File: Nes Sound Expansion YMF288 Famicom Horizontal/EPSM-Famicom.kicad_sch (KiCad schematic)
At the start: 39 parts

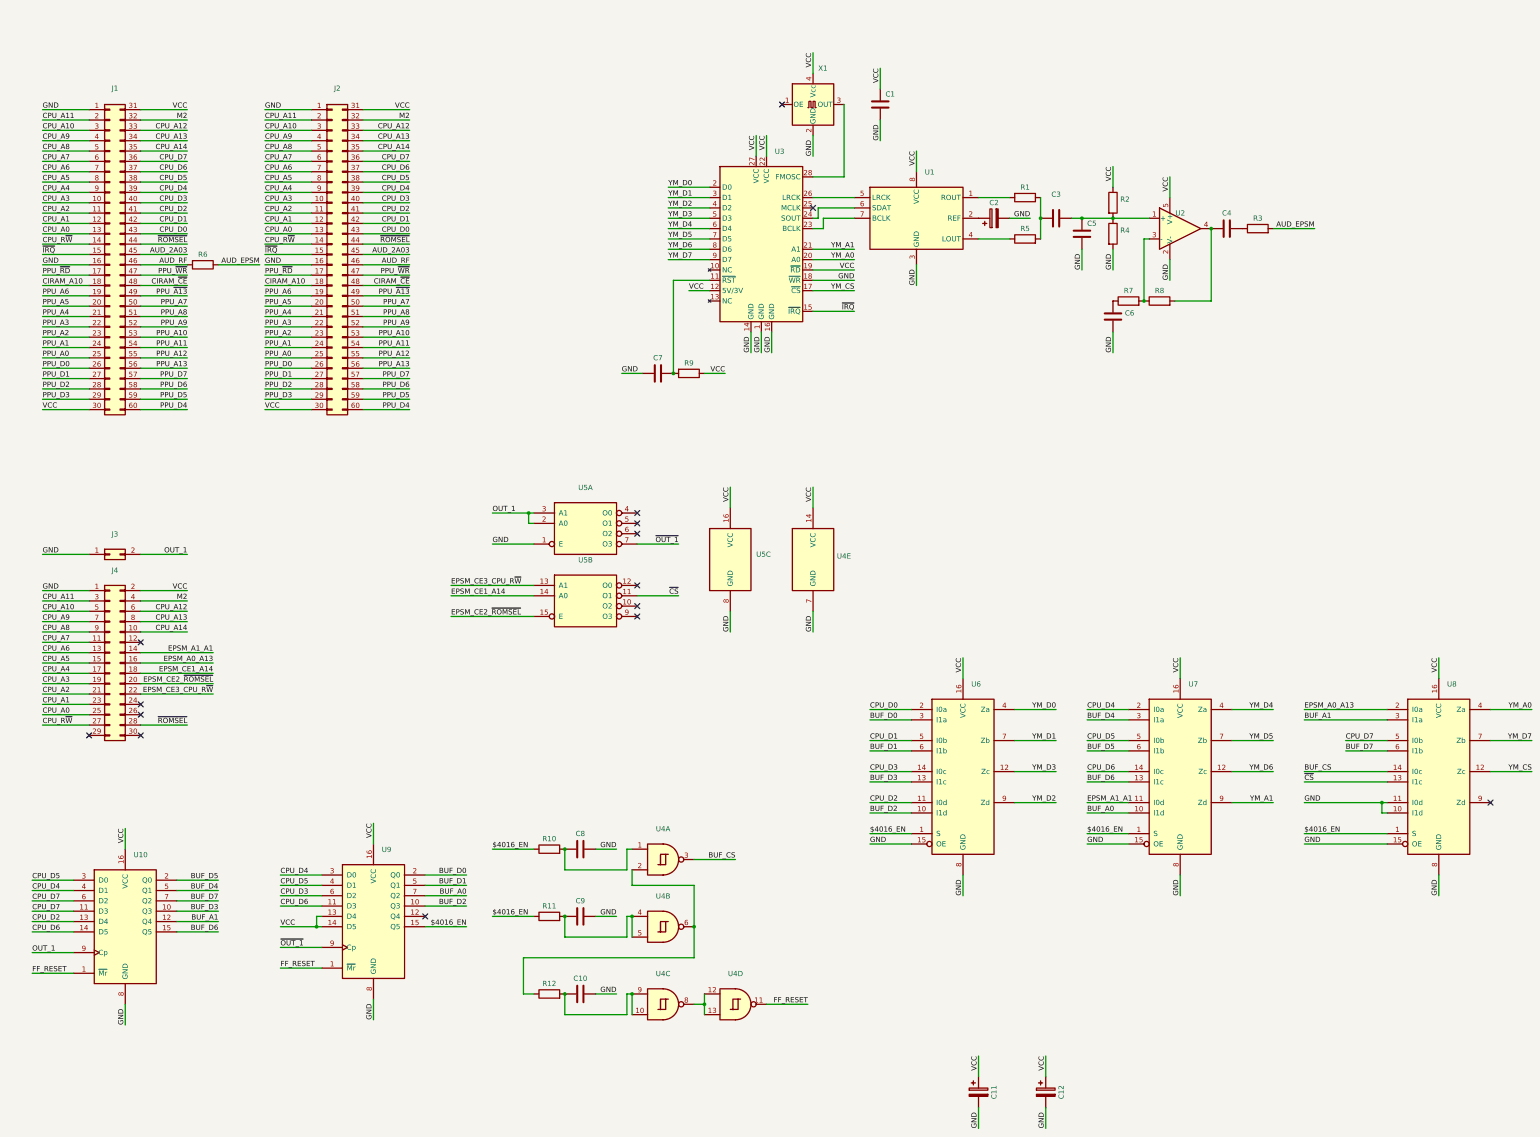
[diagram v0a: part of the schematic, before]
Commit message: Flip cartridge connection to back instead of front
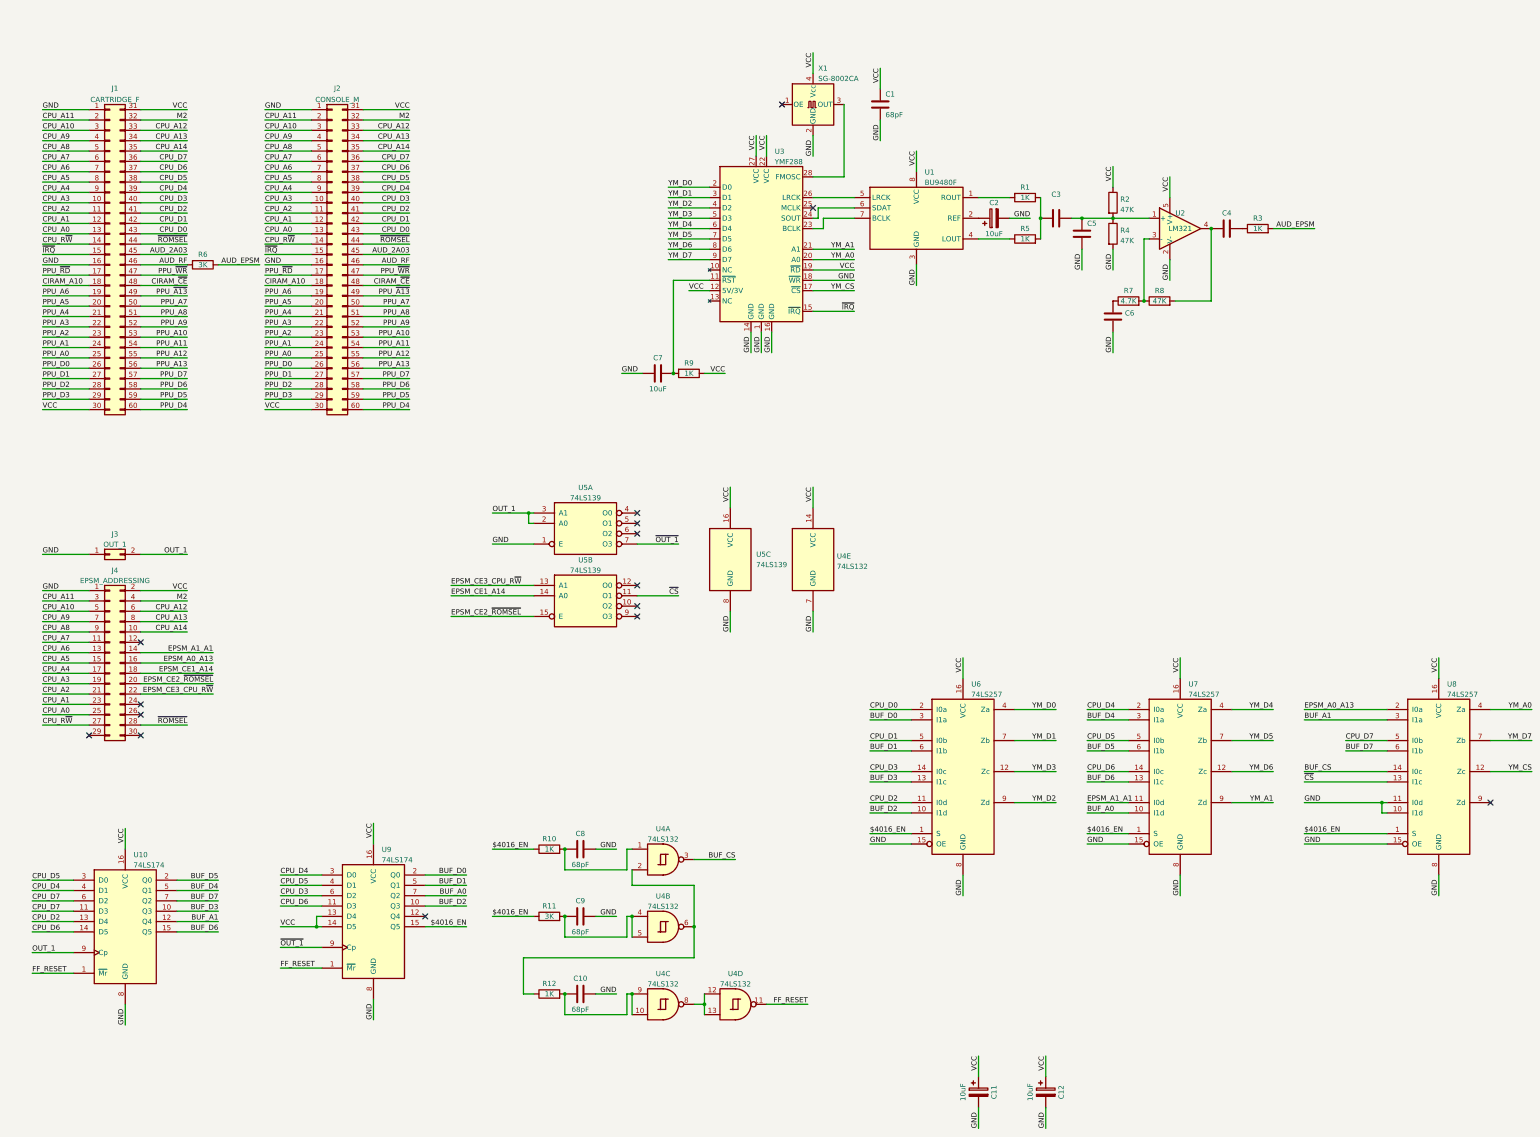
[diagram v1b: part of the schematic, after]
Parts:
- C1, C10, C8, C9: value (none) -> 68pF; footprint (none) -> Capacitor_SMD:C_0805_2012Metric_Pad1.18x1.45mm_HandSolder
- C11, C12, C2: value (none) -> 10uF; footprint (none) -> Capacitor_SMD:CP_Elec_4x5.3
- C7: value (none) -> 10uF
- J1: value (none) -> CARTRIDGE_F; footprint (none) -> EPSM-Famicom:FC_CONN_F
- J2: value (none) -> CONSOLE_M; footprint (none) -> EPSM-Famicom:HVC-ETROM-01
- J3: value (none) -> OUT_1; footprint (none) -> Connector_PinHeader_2.54mm:PinHeader_1x02_P2.54mm_Vertical
- J4: value (none) -> EPSM_ADDRESSING; footprint (none) -> Connector_PinSocket_2.54mm:PinSocket_2x15_P2.54mm_Vertical_SMD
- R1, R10, R12, R3, R5, R9: value (none) -> 1K; footprint (none) -> Resistor_SMD:R_0805_2012Metric_Pad1.20x1.40mm_HandSolder
- R11, R6: value (none) -> 3K; footprint (none) -> Resistor_SMD:R_0805_2012Metric_Pad1.20x1.40mm_HandSolder
- R2, R4, R8: value (none) -> 47K; footprint (none) -> Resistor_SMD:R_0805_2012Metric_Pad1.20x1.40mm_HandSolder
- R7: value (none) -> 4.7K; footprint (none) -> Resistor_SMD:R_0805_2012Metric_Pad1.20x1.40mm_HandSolder
- U1: value (none) -> BU9480F; footprint (none) -> Package_SO:SOIC-8_5.275x5.275mm_P1.27mm
- U10, U9: value (none) -> 74LS174; footprint (none) -> Package_SO:SOIC-16_3.9x9.9mm_P1.27mm
- U2: value (none) -> LM321; footprint (none) -> Package_TO_SOT_SMD:SOT-23-5
- U3: value (none) -> YMF288; footprint (none) -> EPSM-Famicom:SOP-28_7.5x12.8mm_P1.27mm
- U4: value (none) -> 74LS132; footprint (none) -> Package_SO:SOIC-14_3.9x8.7mm_P1.27mm
- U5: value (none) -> 74LS139; footprint (none) -> Package_SO:SOIC-16_3.9x9.9mm_P1.27mm
- U6, U7, U8: value (none) -> 74LS257; footprint (none) -> Package_SO:SOIC-16_3.9x9.9mm_P1.27mm
- X1: value (none) -> SG-8002CA; footprint (none) -> Oscillator:Oscillator_SMD_SeikoEpson_SG8002CA-4Pin_7.0x5.0mm

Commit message: Update FC-H EPSM
- Upgrade to 4 layers
- Use same amplifier circuit as NES EPSM
- Optimize logic chip pin assignment
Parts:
- removed C12, C2: 10uF, Capacitor_SMD:CP_Elec_4x5.3, symbol Device:C_Polarized
- removed R5: 1K, Resistor_SMD:R_0805_2012Metric_Pad1.20x1.40mm_HandSolder, symbol Device:R
- removed U2: LM321, Package_TO_SOT_SMD:SOT-23-5, symbol Amplifier_Operational:LM321
- added C1, C10, C12, C13, C2, C22, C23, C26, C7, C8: 0.1uF, Capacitor_SMD:C_0805_2012Metric_Pad1.18x1.45mm_HandSolder, symbol Device:C
- added C11, C17, C21, C25: 10uF, Capacitor_SMD:C_0805_2012Metric_Pad1.18x1.45mm_HandSolder, symbol Device:C
- added C14: 100uF, Capacitor_THT:CP_Radial_D5.0mm_P2.50mm, symbol Device:C_Polarized
- added C19: 68pF, Capacitor_SMD:C_0805_2012Metric_Pad1.18x1.45mm_HandSolder, symbol Device:C
- added J5: AudioJack4_SwitchTR1, EPSM-Famicom:Jack_3.5mm_PJ311_Horizontal, symbol Connector:AudioJack4_SwitchTR1
- added R11, R12: 47K, Resistor_SMD:R_0805_2012Metric_Pad1.20x1.40mm_HandSolder, symbol Device:R
- added R14: 8.2K, Resistor_SMD:R_0805_2012Metric_Pad1.20x1.40mm_HandSolder, symbol Device:R
- added R16: 22K, Resistor_SMD:R_0805_2012Metric_Pad1.20x1.40mm_HandSolder, symbol Device:R
- added R6: 3K, Resistor_SMD:R_0805_2012Metric_Pad1.20x1.40mm_HandSolder, symbol Device:R
- added R7: 680, Resistor_SMD:R_0805_2012Metric_Pad1.20x1.40mm_HandSolder, symbol Device:R
- added U9: LM358, Package_SO:SOIC-8_3.9x4.9mm_P1.27mm, symbol Amplifier_Operational:LM358
- C15: renamed from C11; value 10uF -> 100uF; footprint Capacitor_SMD:CP_Elec_4x5.3 -> Capacitor_THT:CP_Radial_D5.0mm_P2.50mm
- C16: renamed from C3; value (none) -> 10uF; footprint (none) -> Capacitor_SMD:C_0805_2012Metric_Pad1.18x1.45mm_HandSolder
- C18: renamed from C5; value (none) -> 68pF; footprint (none) -> Capacitor_SMD:C_0805_2012Metric_Pad1.18x1.45mm_HandSolder
- C20: renamed from C6; value (none) -> 10uF; footprint (none) -> Capacitor_SMD:C_0805_2012Metric_Pad1.18x1.45mm_HandSolder
- C24: renamed from C4; value (none) -> 10uF; footprint (none) -> Capacitor_SMD:C_0805_2012Metric_Pad1.18x1.45mm_HandSolder
- C6: renamed from C7; footprint (none) -> Capacitor_SMD:C_0805_2012Metric_Pad1.18x1.45mm_HandSolder
- R13: renamed from R7; value 4.7K -> 8.2K
- R15: renamed from R8; value 47K -> 22K
- R5: renamed from R1; value 1K -> 680
- renumbered C8 to C3, C9 to C4, C10 to C5, C1 to C9, J3 to J2, J4 to J3, J2 to J4, R10 to R1, R4 to R10, R3 to R17, R11 to R2, R12 to R3, R9 to R4, R6 to R8, R2 to R9, U10 to U1, U8 to U10, U9 to U2, U5 to U3, U3 to U5, U1 to U6, U6 to U7, U7 to U8
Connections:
- net $4016_EN: now also U2.12 (Q4); no longer U2.15 (Q5)
- net AUD_EPSM: now also J4.46 (Pin_46); no longer R8.1
- net AUD_RF: now also R6.2; no longer J4.46 (Pin_46)
- net BUF_A0: now also U1.2 (Q0), U10.13 (I1c); no longer U2.7 (Q2), U8.10 (I1d)
- net BUF_A1: now also U1.5 (Q1), U10.6 (I1b); no longer U1.12 (Q4), U10.3 (I1a)
- net BUF_CS: now also U10.2 (I0a); no longer U10.14 (I0c)
- net BUF_D0: now also U2.10 (Q3), U7.13 (I1c); no longer U2.2 (Q0), U7.3 (I1a)
- net BUF_D1: now also U2.7 (Q2); no longer U2.5 (Q1)
- net BUF_D2: now also U2.5 (Q1), U7.3 (I1a); no longer U2.10 (Q3), U7.10 (I1d)
- net BUF_D3: now also U2.2 (Q0), U8.10 (I1d); no longer U1.10 (Q3), U7.13 (I1c)
- net BUF_D4: now also U1.12 (Q4), U8.13 (I1c); no longer U1.5 (Q1), U8.3 (I1a)
- net BUF_D5: now also U1.10 (Q3); no longer U1.2 (Q0)
- net BUF_D6: now also U8.3 (I1a); no longer U8.13 (I1c)
- net BUF_D7: now also U10.10 (I1d); no longer U10.6 (I1b)
- net CPU_D0: now also U7.14 (I0c); no longer U7.2 (I0a)
- net CPU_D2: now also U1.4 (D1), U7.2 (I0a); no longer U1.13 (D4), U7.11 (I0d)
- net CPU_D3: now also U1.3 (D0), U8.11 (I0d); no longer U2.6 (D2), U7.14 (I0c)
- net CPU_D4: now also U1.13 (D4), U2.11 (D3), U8.14 (I0c); no longer U1.4 (D1), U2.3 (D0), U8.2 (I0a)
- net CPU_D5: now also U1.11 (D3), U2.6 (D2); no longer U1.3 (D0), U2.4 (D1)
- net CPU_D6: now also U2.4 (D1), U8.2 (I0a); no longer U2.11 (D3), U8.14 (I0c)
- net CPU_D7: now also U10.11 (I0d), U2.3 (D0); no longer U1.11 (D3), U10.5 (I0b)
- net EPSM_A0_A13: now also U10.5 (I0b); no longer U10.2 (I0a)
- net EPSM_A1_A1: now also U10.14 (I0c); no longer U8.11 (I0d)
- net EPSM_CE1_A14: now also U3.2 (A0); no longer U3.14 (A0)
- net EPSM_CE2_~{ROMSEL}: now also U3.1 (E); no longer U3.15 (E)
- net EPSM_CE3_CPU_R~{W}: now also U3.3 (A1); no longer U3.13 (A1)
- net FF_RESET: now also U4.8; no longer U4.11
- net GND: now also C20.1, U3.15 (E), U7.10 (I1d), U7.11 (I0d), C1.1, C10.1, C11.2, C12.1, C13.1, C14.2, C19.2, C2.1, C21.1, C22.1, C23.1, C26.1, C7.1, C8.1, J5.S, R12.2, U9.4 (V-); no longer C20.2, U10.10 (I1d), U10.11 (I0d), U3.1 (E)
- net OUT_1: now also U3.13 (A1), U3.14 (A0); no longer U3.2 (A0), U3.3 (A1)
- net VCC: now also C1.2, C10.2, C12.2, C13.2, C14.1, C2.2, C22.2, C23.2, C26.2, C7.2, C8.2, R11.1, U9.8 (V+)
- net YM_A0: now also U10.7 (Zb); no longer U10.4 (Za)
- net YM_A1: now also U10.12 (Zc); no longer U8.9 (Zd)
- net YM_CS: now also U10.4 (Za); no longer U10.12 (Zc)
- net YM_D0: now also U7.12 (Zc); no longer U7.4 (Za)
- net YM_D2: now also U7.4 (Za); no longer U7.9 (Zd)
- net YM_D3: now also U8.9 (Zd); no longer U7.12 (Zc)
- net YM_D4: now also U8.12 (Zc); no longer U8.4 (Za)
- net YM_D6: now also U8.4 (Za); no longer U8.12 (Zc)
- net YM_D7: now also U10.9 (Zd); no longer U10.7 (Zb)
- net ~{CS}: now also U10.3 (I1a), U3.5 (O1); no longer U10.13 (I1c), U3.11 (O1)
- net ~{OUT_1}: now also U3.9 (O3); no longer U3.7 (O3)
- net at R17.1: now also J5.R1N, J5.TN; no longer C24.2
- net at R13.1: now also C20.2; no longer C20.1
- net at R13.2, R15.1: now also U9.2 (-)
- net at C24.1, R15.2: now also U9.1
- net at U4.12, U4.13: now also C5.1, R3.2; no longer U4.8
- net at U6.2 (REF): now also C11.1
- net at C16.2, C18.1, R10.1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: now also U9.3 (+)
- net at U4.10, U4.9: now also U4.11; no longer C5.1, R3.2
- net at C16.1, R5.1: now also R6.1
- net at U6.4 (LOUT): now also R7.2
- new net: C21.2, R14.1
- new net: R14.2, R16.1, U9.6 (-)
- new net: C17.1, R7.1, R8.1
- new net: C17.2, C19.1, R11.2, R12.1, U9.5 (+)
- new net: C25.1, R16.2, U9.7
- new net: C24.2, J5.T
- new net: C25.2, J5.R1
- no-connect marks 15 -> 16
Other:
- moved on the sheet: C15, C16, C18, C20, C24, C6, C9, R10, R13, R15, R17, R4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

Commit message: Reposition all SMD components to be on top
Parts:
- X1: footprint Oscillator:Oscillator_SMD_SeikoEpson_SG8002CA-4Pin_7.0x5.0mm -> Oscillator:Oscillator_SMD_SeikoEpson_SG8002LB-4Pin_5.0x3.2mm
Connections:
- net BUF_A0: now also U2.7 (Q2), U7.3 (I1a); no longer U1.2 (Q0), U10.13 (I1c)
- net BUF_A1: now also U2.10 (Q3), U7.6 (I1b); no longer U1.5 (Q1), U10.6 (I1b)
- net BUF_CS: now also U7.14 (I0c); no longer U10.2 (I0a)
- net BUF_D0: now also U1.2 (Q0), U10.3 (I1a); no longer U2.10 (Q3), U7.13 (I1c)
- net BUF_D1: now also U1.5 (Q1), U10.6 (I1b); no longer U2.7 (Q2), U7.6 (I1b)
- net BUF_D2: now also U1.7 (Q2), U10.13 (I1c); no longer U2.5 (Q1), U7.3 (I1a)
- net BUF_D3: now also U1.15 (Q5), U10.10 (I1d); no longer U2.2 (Q0), U8.10 (I1d)
- net BUF_D4: now also U8.3 (I1a); no longer U8.13 (I1c)
- net BUF_D6: now also U2.2 (Q0), U8.13 (I1c); no longer U1.15 (Q5), U8.3 (I1a)
- net BUF_D7: now also U2.5 (Q1), U8.10 (I1d); no longer U1.7 (Q2), U10.10 (I1d)
- net CPU_D0: now also U10.2 (I0a); no longer U7.14 (I0c)
- net CPU_D1: now also U10.5 (I0b); no longer U7.5 (I0b)
- net CPU_D2: now also U10.14 (I0c), U2.11 (D3); no longer U1.4 (D1), U7.2 (I0a)
- net CPU_D3: now also U10.11 (I0d), U2.6 (D2); no longer U1.3 (D0), U8.11 (I0d)
- net CPU_D4: now also U1.3 (D0), U8.2 (I0a); no longer U2.11 (D3), U8.14 (I0c)
- net CPU_D5: now also U1.4 (D1); no longer U2.6 (D2)
- net CPU_D6: now also U1.6 (D2), U2.3 (D0), U8.14 (I0c); no longer U1.14 (D5), U2.4 (D1), U8.2 (I0a)
- net CPU_D7: now also U1.14 (D5), U2.4 (D1), U8.11 (I0d); no longer U1.6 (D2), U10.11 (I0d), U2.3 (D0)
- net EPSM_A0_A13: now also U7.5 (I0b); no longer U10.5 (I0b)
- net EPSM_A1_A1: now also U7.2 (I0a); no longer U10.14 (I0c)
- net YM_A0: now also U7.7 (Zb); no longer U10.7 (Zb)
- net YM_A1: now also U7.4 (Za); no longer U10.12 (Zc)
- net YM_CS: now also U7.12 (Zc); no longer U10.4 (Za)
- net YM_D0: now also U10.4 (Za); no longer U7.12 (Zc)
- net YM_D1: now also U10.7 (Zb); no longer U7.7 (Zb)
- net YM_D2: now also U10.12 (Zc); no longer U7.4 (Za)
- net YM_D3: now also U10.9 (Zd); no longer U8.9 (Zd)
- net YM_D4: now also U8.4 (Za); no longer U8.12 (Zc)
- net YM_D6: now also U8.12 (Zc); no longer U8.4 (Za)
- net YM_D7: now also U8.9 (Zd); no longer U10.9 (Zd)
- net ~{CS}: now also U7.13 (I1c); no longer U10.3 (I1a)
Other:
- moved on the sheet: C13, C26, U10, U7
